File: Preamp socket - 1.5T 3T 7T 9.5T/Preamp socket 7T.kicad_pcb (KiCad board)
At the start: 2 copper layers, 23 x 17.8 mm, 12 parts, among them J1 In, J2 VCC, J3 Out, J4 GND, U1 Preamp

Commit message: Updated 3D settings
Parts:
- added REF**: Shield_15mm_20mm, _Custom:Shield_15mm_20mm, F.Cu at (157.1, 99.0)
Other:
- board text added: "03/2020 v0.2"
- board text removed: "02/2020 v0.1"

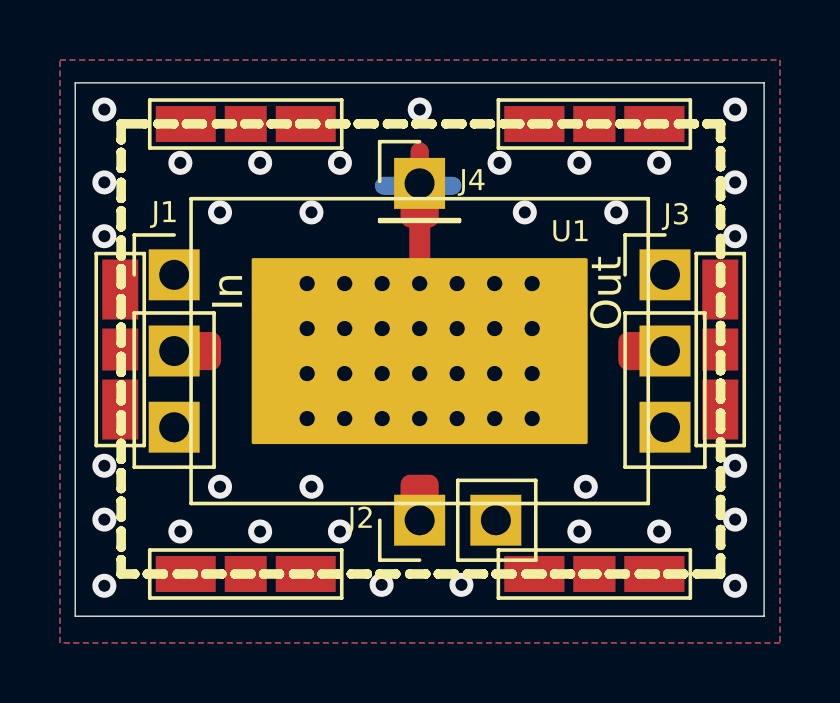
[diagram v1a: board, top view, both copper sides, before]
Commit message: Changed: header hole size, header to preci-dip header
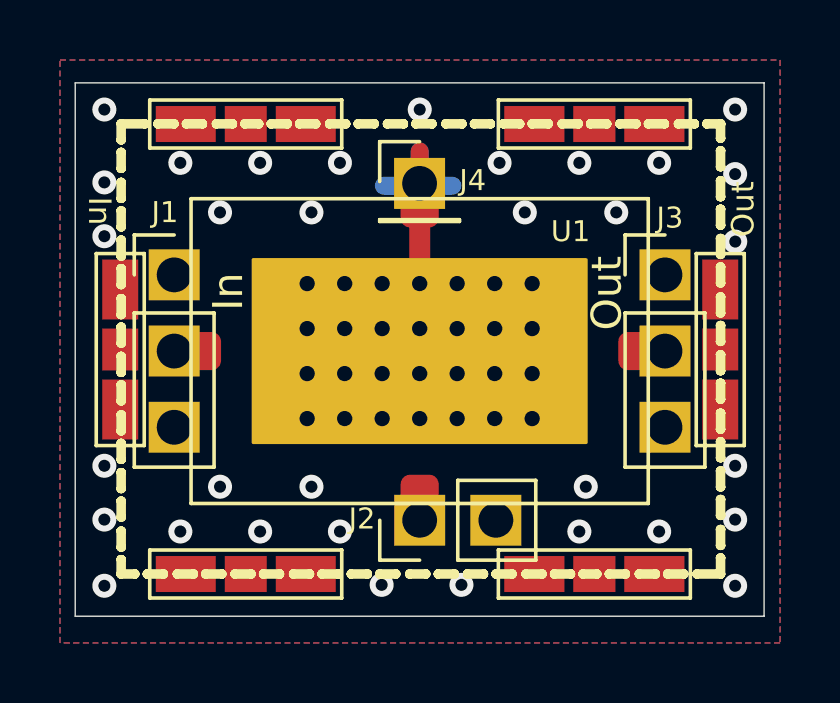
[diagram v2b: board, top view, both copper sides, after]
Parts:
- J1, J3: footprint _Custom_footprints:PinHeader_1x03_P2.54mm_Vertical_rectangular -> _Custom:Preci-dip_PinHeader_1x03_rect
- J2: footprint Connector_PinHeader_2.54mm:PinHeader_1x02_P2.54mm_Vertical -> _Custom:Preci-dip_PinHeader_1x02_rect
- J4: footprint Connector_PinHeader_2.54mm:PinHeader_1x01_P2.54mm_Vertical -> _Custom:Preci-dip_PinHeader_1x01_rect
- moved G1 0.65 mm to (164.0, 93.1)
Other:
- board text added: "Preamp socket 7T"
- board text removed: "Preamp socket"
